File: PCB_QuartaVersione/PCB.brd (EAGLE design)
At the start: 41 x 41 mm, 55 parts, among them Q1 BSS138, Q2 BSS138, Q3 BSS138, Q4 BSS138

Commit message: modifiche per vedere connessione
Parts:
- removed R19, R20: ERJ-2GEJ515X, Res_5,1M_0402:RESC1005X40N
- added R1, R2: ERJ-2GEJ106X, Res_10M_0402:RESC1005X40N
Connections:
- net BATTERY: now also R1.1, R2.1; no longer R19.2, R20.2
- net GND: now also R2.2; no longer R20.1
- net VDD: now also R1.2; no longer R19.1
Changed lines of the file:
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@@
 <attribute name="PURCHASE-URL" value="https://pricing.snapeda.com/search/part/ERJ-2GEJ515X/?ref=eda" x="32.1" y="32.5" size="1.778" layer="27" rot="R270" display="off"/>
-</element>
-<element name="R19" library="Res_5,1M_0402" package="RESC1005X40N" value="ERJ-2GEJ515X" x="32.5" y="45.7" smashed="yes" rot="MR270">
-<attribute name="DESCRIPTION" value=" 5.1 MOhms ±5% 0.1W, 1/10W Chip Resistor 0402 (1005 Metric) Automotive AEC-Q200 Thick Film " x="32.5" y="45.7" size="1.778" layer="28" rot="MR270" display="off"/>
-<attribute name="DIGI-KEY_PART_NUMBER" value="P5.1MJTR-ND" x="32.5" y="45.7" size="1.778" layer="28" rot="MR270" display="off"/>
-<attribute name="MF" value="Panasonic" x="32.5" y="45.7" size="1.778" layer="28" rot="MR270" display="off"/>
-<attribute name="MP" value="ERJ-2GEJ515X" x="32.5" y="45.7" size="1.778" layer="28" rot="MR270" display="off"/>
-<attribute name="NAME" x="30.83" y="43.55" size="1" layer="22" rot="MR90"/>
-<attribute name="PACKAGE" value="1005 Panasonic Electronic Components" x="32.5" y="45.7" size="1.778" layer="28" rot="MR270" display="off"/>
-<attribute name="PURCHASE-URL" value="https://pricing.snapeda.com/search/part/ERJ-2GEJ515X/?ref=eda" x="32.5" y="45.7" size="1.778" layer="28" rot="MR270" display="off"/>
-</element>
-<element name="R20" library="Res_5,1M_0402" package="RESC1005X40N" value="ERJ-2GEJ515X" x="33.4" y="43" smashed="yes" rot="MR90">
-<attribute name="DESCRIPTION" value=" 5.1 MOhms ±5% 0.1W, 1/10W Chip Resistor 0402 (1005 Metric) Automotive AEC-Q200 Thick Film " x="33.4" y="43" size="1.778" layer="28" rot="MR90" display="off"/>
-<attribute name="DIGI-KEY_PART_NUMBER" value="P5.1MJTR-ND" x="33.4" y="43" size="1.778" layer="28" rot="MR90" display="off"/>
-<attribute name="MF" value="Panasonic" x="33.4" y="43" size="1.778" layer="28" rot="MR90" display="off"/>
-<attribute name="MP" value="ERJ-2GEJ515X" x="33.4" y="43" size="1.778" layer="28" rot="MR90" display="off"/>
-<attribute name="NAME" x="33.05" y="41.87" size="1" layer="22" rot="MR180"/>
-<attribute name="PACKAGE" value="1005 Panasonic Electronic Components" x="33.4" y="43" size="1.778" layer="28" rot="MR90" display="off"/>
-<attribute name="PURCHASE-URL" value="https://pricing.snapeda.com/search/part/ERJ-2GEJ515X/?ref=eda" x="33.4" y="43" size="1.778" layer="28" rot="MR90" display="off"/>
 </element>
 <element name="C1" library="Cond_100n_0402" package="CAPC1005X55N" value="C0402C104K9RACAUTO" x="32" y="47.8" smashed="yes" rot="MR90">
@@
 <attribute name="PACKAGE" value="1005 AVX" x="31.6" y="44.8" size="1.778" layer="27" rot="R180" display="off"/>
 <attribute name="PURCHASE-URL" value="https://pricing.snapeda.com/search/part/04025A120FAT2A/?ref=eda" x="31.6" y="44.8" size="1.778" layer="27" rot="R180" display="off"/>
+</element>
+<element name="R1" library="Res_10M_0402" package="RESC1005X40N" value="ERJ-2GEJ106X" x="32.5" y="45.7" smashed="yes" rot="MR90">
+<attribute name="DESCRIPTION" value=" Res Thick Film 0402 10M Ohm 5% 1/10W -400ppm/°C to 150ppm/°C Molded SMD Punched Carrier T/R " x="32.5" y="45.7" size="1.778" layer="28" rot="MR90" display="off"/>
+<attribute name="DIGI-KEY_PART_NUMBER" value="P10MJTR-ND" x="32.5" y="45.7" size="1.778" layer="28" rot="MR90" display="off"/>
+<attribute name="MF" value="Panasonic Electronic" x="32.5" y="45.7" size="1.778" layer="28" rot="MR90" display="off"/>
+<attribute name="MP" value="ERJ-2GEJ106X" x="32.5" y="45.7" size="1.778" layer="28" rot="MR90" display="off"/>
+<attribute name="NAME" x="33.13" y="44.75" size="0.5" layer="26" rot="MR90"/>
+<attribute name="PACKAGE" value="1005 Panasonic Electronic Components" x="32.5" y="45.7" size="1.778" layer="28" rot="MR90" display="off"/>
+<attribute name="PURCHASE-URL" value="https://pricing.snapeda.com/search/part/ERJ-2GEJ106X/?ref=eda" x="32.5" y="45.7" size="1.778" layer="28" rot="MR90" display="off"/>
+<attribute name="VALUE" x="31.87" y="44.75" size="0.5" layer="28" rot="MR90" align="top-left"/>
+</element>
+<element name="R2" library="Res_10M_0402" package="RESC1005X40N" value="ERJ-2GEJ106X" x="33.4" y="43" smashed="yes" rot="MR270">
+<attribute name="DESCRIPTION" value=" Res Thick Film 0402 10M Ohm 5% 1/10W -400ppm/°C to 150ppm/°C Molded SMD Punched Carrier T/R " x="33.4" y="43" size="1.778" layer="28" rot="MR270" display="off"/>
+<attribute name="DIGI-KEY_PART_NUMBER" value="P10MJTR-ND" x="33.4" y="43" size="1.778" layer="28" rot="MR270" display="off"/>
+<attribute name="MF" value="Panasonic Electronic" x="33.4" y="43" size="1.778" layer="28" rot="MR270" display="off"/>
+<attribute name="MP" value="ERJ-2GEJ106X" x="33.4" y="43" size="1.778" layer="28" rot="MR270" display="off"/>
+<attribute name="NAME" x="32.77" y="43.95" size="0.5" layer="26" rot="MR270"/>
+<attribute name="PACKAGE" value="1005 Panasonic Electronic Components" x="33.4" y="43" size="1.778" layer="28" rot="MR270" display="off"/>
+<attribute name="PURCHASE-URL" value="https://pricing.snapeda.com/search/part/ERJ-2GEJ106X/?ref=eda" x="33.4" y="43" size="1.778" layer="28" rot="MR270" display="off"/>
+<attribute name="VALUE" x="34.03" y="43.95" size="0.5" layer="28" rot="MR270" align="top-left"/>
 </element>
 </elements>
@@
 <contactref element="R15" pad="2"/>
 <contactref element="R16" pad="1"/>
-<contactref element="R20" pad="1"/>
 <contactref element="C1" pad="2"/>
 <contactref element="C2" pad="2"/>
@@
 <via x="40.6" y="48.6" extent="1-16" drill="0.35" diameter="0.3"/>
 <via x="29.4" y="37.9" extent="1-16" drill="0.35" diameter="0.3"/>
+<contactref element="R2" pad="2"/>
 </signal>
 <signal name="N$11">
@@
 <wire x1="39.1" y1="49.6" x2="33.4" y2="49.6" width="0.254" layer="16"/>
 <wire x1="38.178" y1="47.5251" x2="38.178" y2="48.1754" width="0.254" layer="16"/>
-<contactref element="R19" pad="1"/>
 <contactref element="C1" pad="1"/>
 <wire x1="32.8" y1="49" x2="32.8" y2="47.7" width="0.254" layer="16"/>
@@
 <wire x1="48.7" y1="49.1" x2="47.4" y2="49.1" width="0.254" layer="16"/>
 <wire x1="47.4" y1="49.1" x2="47.25" y2="49.25" width="0.254" layer="16"/>
+<contactref element="R1" pad="2"/>
 </signal>
 <signal name="3.3V">
@@
 <wire x1="22.17" y1="41.83" x2="23.6" y2="40.4" width="0.254" layer="1"/>
 <wire x1="23.6" y1="40.4" x2="24.2" y2="40.4" width="0.254" layer="1"/>
-<contactref element="R19" pad="2"/>
-<contactref element="R20" pad="2"/>
 <contactref element="C9" pad="1"/>
 <wire x1="28.53" y1="43.43" x2="32.1" y2="43.43" width="0.254" layer="16"/>
@@
 <wire x1="32.5" y1="45.255" x2="32.5" y2="43.83" width="0.254" layer="16"/>
 <wire x1="32.5" y1="43.83" x2="32.1" y2="43.43" width="0.254" layer="16"/>
+<contactref element="R2" pad="1"/>
+<contactref element="R1" pad="1"/>
 </signal>
 <signal name="BJT">

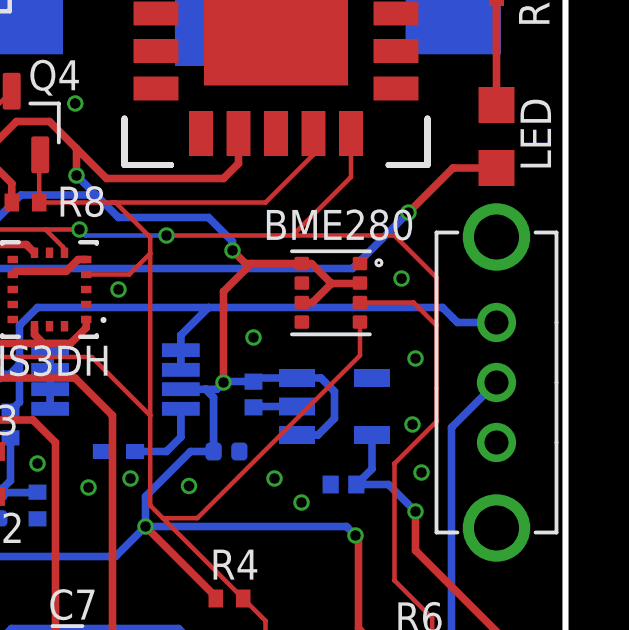
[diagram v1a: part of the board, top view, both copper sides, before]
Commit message: Aggiunta geolocalizzazione e salvata su file
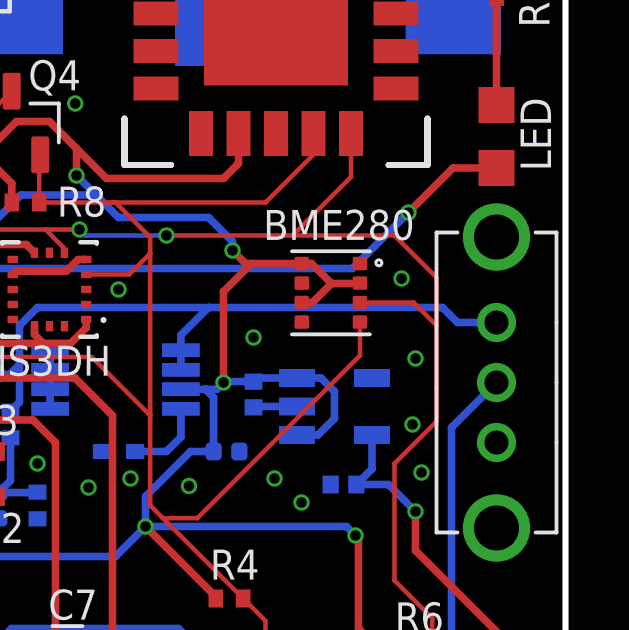
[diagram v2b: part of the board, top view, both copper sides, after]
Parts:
- renumbered R1 to R19, R2 to R20
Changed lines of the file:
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@@
 <grid distance="1" unitdist="mm" unit="mm" style="lines" multiple="1" display="yes" altdistance="0.1" altunitdist="mm" altunit="mm"/>
 <layers>
-<layer number="1" name="Top" color="4" fill="1" visible="yes" active="yes"/>
+<layer number="1" name="Top" color="4" fill="1" visible="no" active="yes"/>
 <layer number="16" name="Bottom" color="1" fill="1" visible="yes" active="yes"/>
 <layer number="17" name="Pads" color="2" fill="1" visible="yes" active="yes"/>
@@
 <layer number="23" name="tOrigins" color="15" fill="1" visible="yes" active="yes"/>
 <layer number="24" name="bOrigins" color="15" fill="1" visible="yes" active="yes"/>
-<layer number="25" name="tNames" color="7" fill="1" visible="no" active="yes"/>
-<layer number="26" name="bNames" color="7" fill="1" visible="no" active="yes"/>
+<layer number="25" name="tNames" color="7" fill="1" visible="yes" active="yes"/>
+<layer number="26" name="bNames" color="7" fill="1" visible="yes" active="yes"/>
 <layer number="27" name="tValues" color="7" fill="1" visible="no" active="yes"/>
 <layer number="28" name="bValues" color="7" fill="1" visible="no" active="yes"/>
@@
 <attribute name="PURCHASE-URL" value="https://pricing.snapeda.com/search/part/04025A120FAT2A/?ref=eda" x="31.6" y="44.8" size="1.778" layer="27" rot="R180" display="off"/>
 </element>
-<element name="R1" library="Res_10M_0402" package="RESC1005X40N" value="ERJ-2GEJ106X" x="32.5" y="45.7" smashed="yes" rot="MR90">
+<element name="R19" library="Res_10M_0402" package="RESC1005X40N" value="ERJ-2GEJ106X" x="32.5" y="45.7" smashed="yes" rot="MR90">
 <attribute name="DESCRIPTION" value=" Res Thick Film 0402 10M Ohm 5% 1/10W -400ppm/°C to 150ppm/°C Molded SMD Punched Carrier T/R " x="32.5" y="45.7" size="1.778" layer="28" rot="MR90" display="off"/>
 <attribute name="DIGI-KEY_PART_NUMBER" value="P10MJTR-ND" x="32.5" y="45.7" size="1.778" layer="28" rot="MR90" display="off"/>
 <attribute name="MF" value="Panasonic Electronic" x="32.5" y="45.7" size="1.778" layer="28" rot="MR90" display="off"/>
 <attribute name="MP" value="ERJ-2GEJ106X" x="32.5" y="45.7" size="1.778" layer="28" rot="MR90" display="off"/>
-<attribute name="NAME" x="33.13" y="44.75" size="0.5" layer="26" rot="MR90"/>
+<attribute name="NAME" x="33.13" y="44.75" size="1" layer="22" rot="MR90"/>
 <attribute name="PACKAGE" value="1005 Panasonic Electronic Components" x="32.5" y="45.7" size="1.778" layer="28" rot="MR90" display="off"/>
 <attribute name="PURCHASE-URL" value="https://pricing.snapeda.com/search/part/ERJ-2GEJ106X/?ref=eda" x="32.5" y="45.7" size="1.778" layer="28" rot="MR90" display="off"/>
 <attribute name="VALUE" x="31.87" y="44.75" size="0.5" layer="28" rot="MR90" align="top-left"/>
 </element>
-<element name="R2" library="Res_10M_0402" package="RESC1005X40N" value="ERJ-2GEJ106X" x="33.4" y="43" smashed="yes" rot="MR270">
+<element name="R20" library="Res_10M_0402" package="RESC1005X40N" value="ERJ-2GEJ106X" x="33.4" y="43" smashed="yes" rot="MR270">
 <attribute name="DESCRIPTION" value=" Res Thick Film 0402 10M Ohm 5% 1/10W -400ppm/°C to 150ppm/°C Molded SMD Punched Carrier T/R " x="33.4" y="43" size="1.778" layer="28" rot="MR270" display="off"/>
 <attribute name="DIGI-KEY_PART_NUMBER" value="P10MJTR-ND" x="33.4" y="43" size="1.778" layer="28" rot="MR270" display="off"/>
 <attribute name="MF" value="Panasonic Electronic" x="33.4" y="43" size="1.778" layer="28" rot="MR270" display="off"/>
 <attribute name="MP" value="ERJ-2GEJ106X" x="33.4" y="43" size="1.778" layer="28" rot="MR270" display="off"/>
-<attribute name="NAME" x="32.77" y="43.95" size="0.5" layer="26" rot="MR270"/>
+<attribute name="NAME" x="34.87" y="44.55" size="1" layer="22" rot="MR270"/>
 <attribute name="PACKAGE" value="1005 Panasonic Electronic Components" x="33.4" y="43" size="1.778" layer="28" rot="MR270" display="off"/>
 <attribute name="PURCHASE-URL" value="https://pricing.snapeda.com/search/part/ERJ-2GEJ106X/?ref=eda" x="33.4" y="43" size="1.778" layer="28" rot="MR270" display="off"/>
@@
 <via x="40.6" y="48.6" extent="1-16" drill="0.35" diameter="0.3"/>
 <via x="29.4" y="37.9" extent="1-16" drill="0.35" diameter="0.3"/>
-<contactref element="R2" pad="2"/>
+<contactref element="R20" pad="2"/>
 </signal>
 <signal name="N$11">
@@
 <contactref element="VR_3.3" pad="1"/>
 <contactref element="VR_3.3" pad="2"/>
-<wire x1="47.25" y1="49.25" x2="46.9" y2="49.6" width="0.254" layer="16"/>
+<wire x1="47.4" y1="49.1" x2="46.9" y2="49.6" width="0.254" layer="16"/>
 <wire x1="46.9" y1="49.6" x2="39.1" y2="49.6" width="0.254" layer="16"/>
 <wire x1="39.1" y1="49.6" x2="33.4" y2="49.6" width="0.254" layer="16"/>
@@
 <contactref element="S1" pad="3"/>
 <wire x1="48.7" y1="49.1" x2="47.4" y2="49.1" width="0.254" layer="16"/>
-<wire x1="47.4" y1="49.1" x2="47.25" y2="49.25" width="0.254" layer="16"/>
-<contactref element="R1" pad="2"/>
+<contactref element="R19" pad="2"/>
 </signal>
 <signal name="3.3V">
@@
 <wire x1="32.5" y1="45.255" x2="32.5" y2="43.83" width="0.254" layer="16"/>
 <wire x1="32.5" y1="43.83" x2="32.1" y2="43.43" width="0.254" layer="16"/>
-<contactref element="R2" pad="1"/>
-<contactref element="R1" pad="1"/>
+<contactref element="R20" pad="1"/>
+<contactref element="R19" pad="1"/>
 </signal>
 <signal name="BJT">
